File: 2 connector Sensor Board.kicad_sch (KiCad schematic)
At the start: 11 parts, among them J1 SPI, J15 TE 3-2363962-0 Connector, J2 7 pin FPC 0.3mm Panasonic Y3b, J3 free pins, J4 TE 3-2363962-0 Connector, J5 7 pin FPC 0.3mm Panasonic Y3b, J7 JST SH

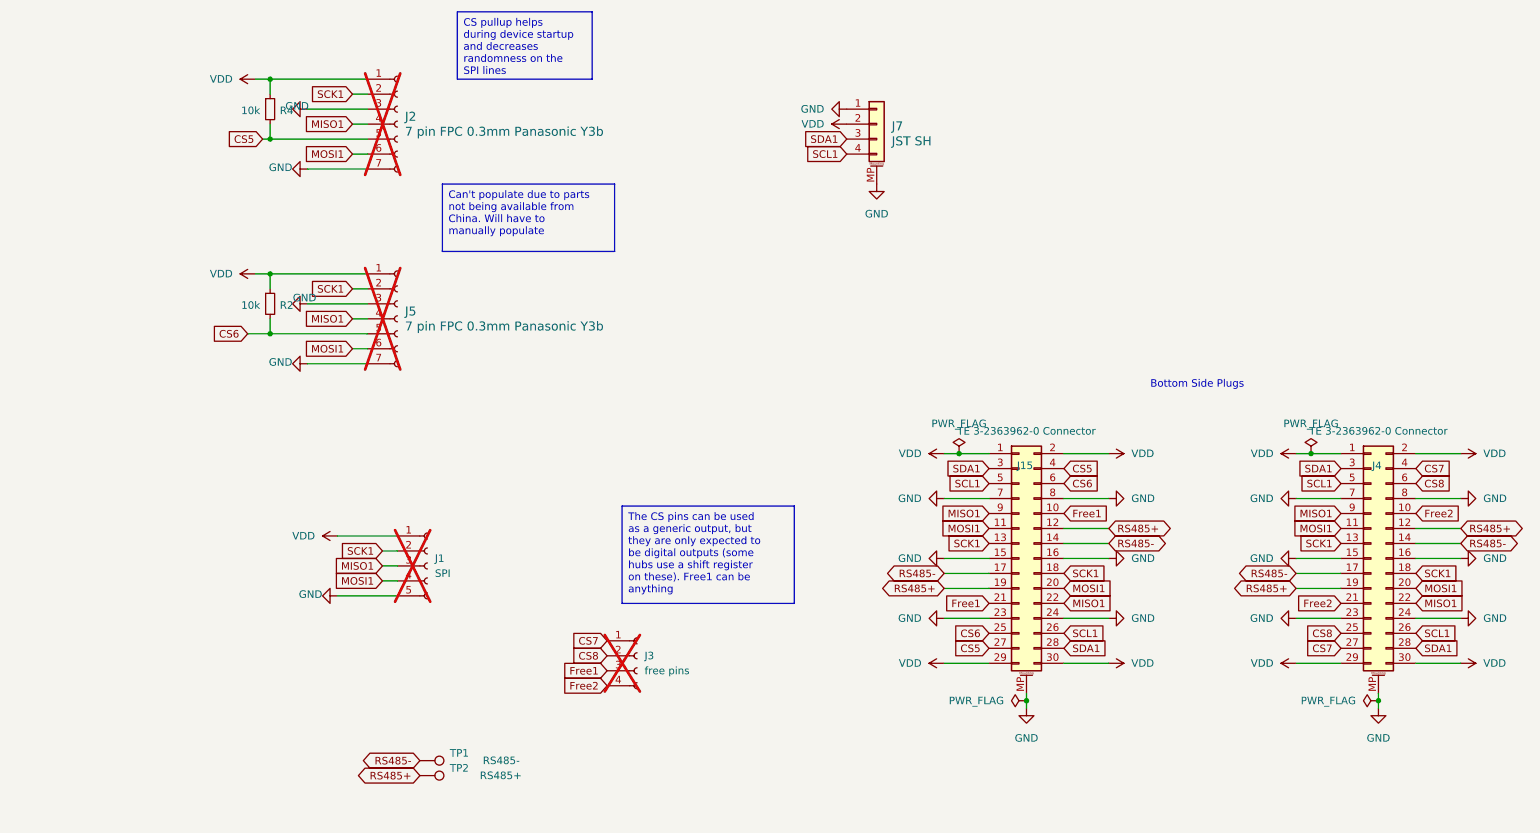
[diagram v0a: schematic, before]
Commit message: Updated schematic with latest parts and pinout
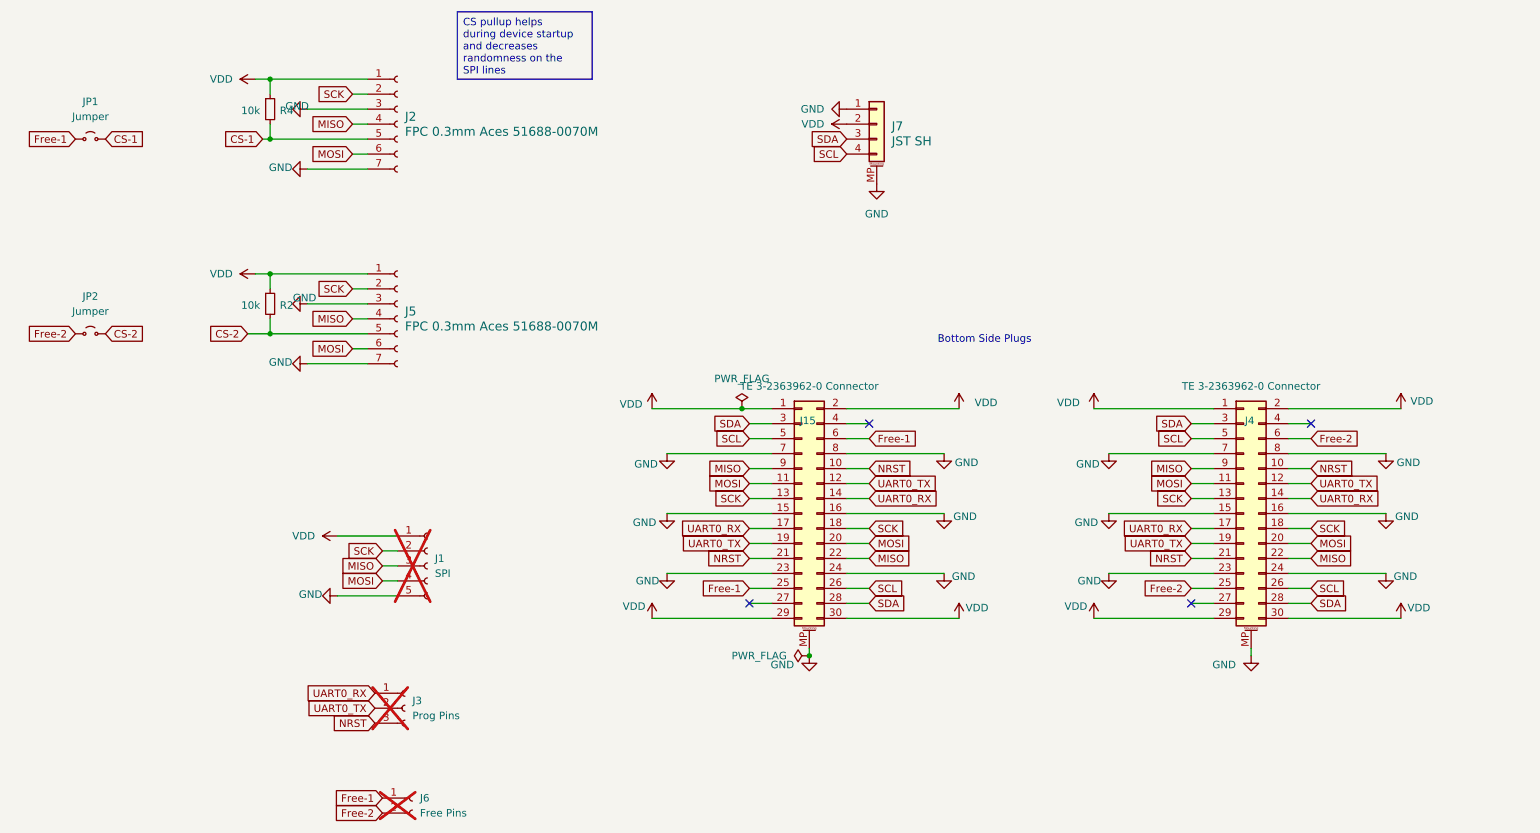
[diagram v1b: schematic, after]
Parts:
- removed TP1: RS485-, TestPoint:TestPoint_Pad_D1.0mm, symbol Connector:TestPoint
- removed TP2: RS485+, TestPoint:TestPoint_Pad_D1.0mm, symbol Connector:TestPoint
- added J6: Free Pins, Connector_PinHeader_1.27mm:PinHeader_1x02_P1.27mm_Vertical, symbol Connector:Conn_01x02_Socket
- added JP1, JP2: Jumper, Jumper:SolderJumper-2_P1.3mm_Open_RoundedPad1.0x1.5mm, symbol Jumper:Jumper_2_Small_Open
- J2, J5: value 7 pin FPC 0.3mm Panasonic Y3b -> FPC 0.3mm Aces 51688-0070M; now fitted
- J3: value free pins -> Prog Pins; footprint Connector_PinHeader_1.27mm:PinHeader_1x04_P1.27mm_Vertical -> Connector_PinHeader_1.27mm:PinHeader_1x03_P1.27mm_Vertical; symbol Connector:Conn_01x04_Socket -> Connector:Conn_01x03_Socket
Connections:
- net CS5 renamed CS-1
- net CS-1: now also JP1.2 (B); no longer J15.27 (Pin_27), J15.4 (Pin_4)
- net CS6 renamed CS-2
- net CS-2: now also JP2.2 (B); no longer J15.25 (Pin_25), J15.6 (Pin_6)
- removed net CS7: J3.1 (Pin_1), J4.27 (Pin_27), J4.4 (Pin_4)
- net CS8 renamed Free-2
- net Free-2: now also J6.2 (Pin_2), JP2.1 (A); no longer J3.2 (Pin_2)
- net Free1 renamed NRST
- net NRST: now also J4.10 (Pin_10), J4.21 (Pin_21)
- removed net Free2: J3.4 (Pin_4), J4.10 (Pin_10), J4.21 (Pin_21)
- net MISO1 renamed MISO
- net MOSI1 renamed MOSI
- net RS485+ renamed UART0_TX
- net UART0_TX: now also J3.2 (Pin_2)
- net RS485- renamed UART0_RX
- net UART0_RX: now also J3.1 (Pin_1)
- net SCK1 renamed SCK
- net SCL1 renamed SCL
- net SDA1 renamed SDA
- new net Free-1: J15.25 (Pin_25), J15.6 (Pin_6), J6.1 (Pin_1), JP1.1 (A)
- no-connect marks 0 -> 4
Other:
- company: Author: Asher Edwards -> (none)
- moved on the sheet: J15, J4
